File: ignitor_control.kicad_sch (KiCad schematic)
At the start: 22 parts, among them J13 Conn_02x01, K2 G5Q-1 DC24, K3 G5Q-1 DC24, K4 G5Q-1 DC24, Q10 BSS138, Q4 BSS138, Q5 BSS138, U12 INA187A2

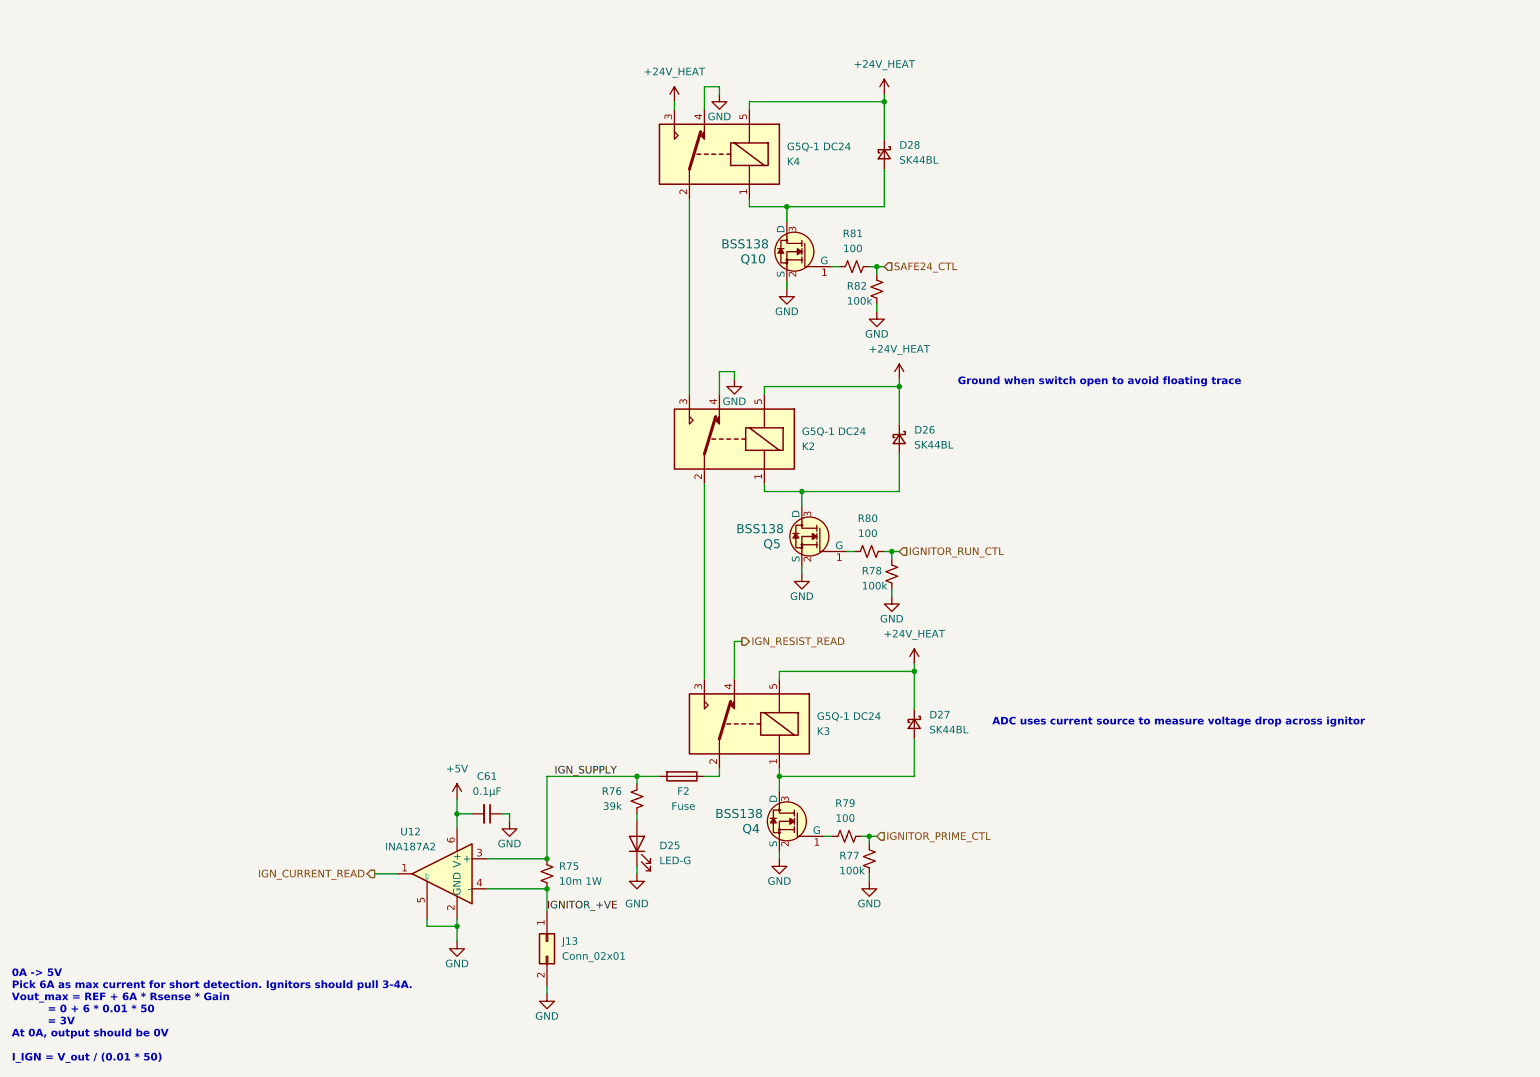
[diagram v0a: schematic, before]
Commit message: add heater power regulation for fet switching
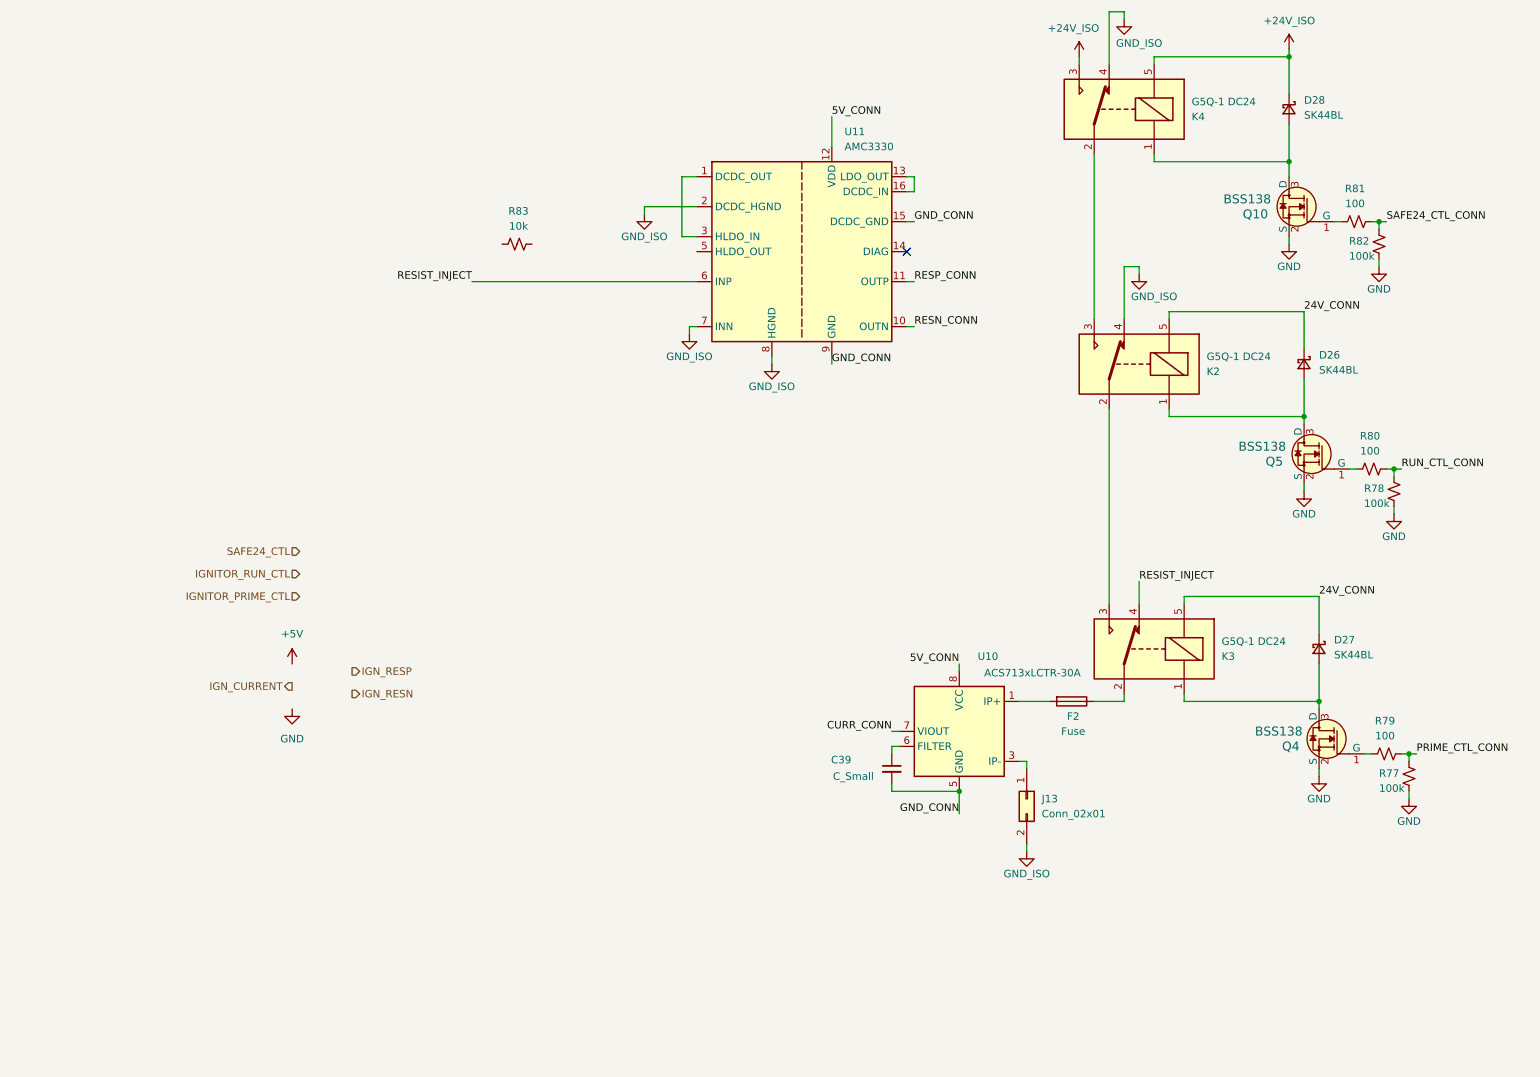
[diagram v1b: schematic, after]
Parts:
- removed C61: 0.1μF, Capacitor_SMD:C_0402_1005Metric, symbol Device:C_Small
- removed D25: LED-G, LED_SMD:LED_0805_2012Metric, symbol Device:LED
- removed R75: 10m 1W, Resistor_SMD:R_1206_3216Metric, symbol Device:R_Small_US
- removed R76: 39k, Resistor_SMD:R_0402_1005Metric, symbol Device:R_Small_US
- removed U12: INA187A2, Package_TO_SOT_SMD:SOT-23-6, symbol Amplifier_Current:INA199xxDCK
- added C39: C_Small, symbol Device:C_Small
- added R83: 10k, Resistor_SMD:R_0402_1005Metric, symbol Device:R_Small_US
- added U10: ACS713xLCTR-30A, Package_SO:SOIC-8_3.9x4.9mm_P1.27mm, symbol Sensor_Current:ACS713xLCTR-30A
- added U11: AMC3330, Package_SO:SOIC-16W_7.5x10.3mm_P1.27mm, symbol Isolator_Analog:AMC3330
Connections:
- net GND: no longer J13.2 (Pin_2), K2.4, K4.4
- net IGNITOR_PRIME_CTL: no longer R77.1, R79.2
- net IGNITOR_RUN_CTL: no longer R78.1, R80.2
- net SAFE24_CTL: no longer R81.2, R82.1
- net +24V_HEAT renamed 24V_CONN
- net 24V_CONN: no longer D28.1 (K), K4.3, K4.5
- net IGNITOR_+VE: no longer names the net of J13.1 (Pin_1)
- net IGNITOR_+VE: now also U10.3 (IP-), U10.4 (IP-)
- net IGN_RESIST_READ renamed RESIST_INJECT
- net RESIST_INJECT: now also U11.6 (INP)
- net IGN_SUPPLY: no longer names the net of F2.2
- net IGN_SUPPLY: now also U10.1 (IP+), U10.2 (IP+)
- new net: C39.1, U10.6 (FILTER)
- new net: U11.1 (DCDC_OUT), U11.3 (HLDO_IN)
- new net: U11.13 (LDO_OUT), U11.16 (DCDC_IN)
- new net +24V_ISO: D28.1 (K), K4.3, K4.5
- new net 5V_CONN: U10.8 (VCC), U11.12 (VDD)
- new net CURR_CONN: U10.7 (VIOUT)
- new net GND_CONN: C39.2, U10.5 (GND), U11.15 (DCDC_GND), U11.9 (GND)
- new net GND_ISO: J13.2 (Pin_2), K2.4, K4.4, U11.2 (DCDC_HGND), U11.7 (INN), U11.8 (HGND)
- new net PRIME_CTL_CONN: R77.1, R79.2
- new net RESN_CONN: U11.10 (OUTN)
- new net RESP_CONN: U11.11 (OUTP)
- new net RUN_CTL_CONN: R78.1, R80.2
- new net SAFE24_CTL_CONN: R81.2, R82.1
- no-connect marks 0 -> 1
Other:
- note removed: "0A -> 5V Pick 6A as max current for short detection. Ignitors should pull 3-4A. Vout_max = REF + 6A * Rsense * Gain = 0 + 6 * 0.01 * 50 = 3V At 0A, output should be 0V I_IGN = V_out / (0.01 * 50)"
- note removed: "ADC uses current source to measure voltage drop across ignitor"
- note removed: "Ground when switch open to avoid floating trace"
- moved on the sheet: D26, D27, D28, F2, J13, K2, K3, K4, Q10, Q4, Q5, R77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
